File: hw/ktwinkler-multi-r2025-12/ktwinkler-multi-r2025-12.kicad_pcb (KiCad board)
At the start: 4 copper layers, 64 x 58 mm, 93 parts, among them J1 USB_C_Receptacle_USB2.0_16P, J10 Conn_01x06, J11 Conn_01x02, J12 Connector_HAN_P1, J13 Conn_01x02, J14 Conn_01x02, J15 Conn_01x02, J16 Conn_01x02, J17 Conn_01x02, J18 Conn_01x02, J19 Conn_01x06, J2 Conn_01x02, J4 Conn_01x02, J5 Conn_01x03, J6 Conn_01x02, J7 Conn_01x02, J8 Conn_01x02, J9 BWU.FL-IPEX1, Q1 HL3400A, Q3 HL2301A, Q4 HL3400A, SW1 RESET, SW2 BOOT, SW5 MODE, U1 TPS631000DRLR, U2 FM116C, U3 ESP32-C3FH4, U4 T1016H, U5 AD116, U6 Protection_H5VU25UC, U8 CH584F, U9 GM8023B, Y1 40M, Y2 32k, Y4 32k, Y5 32M

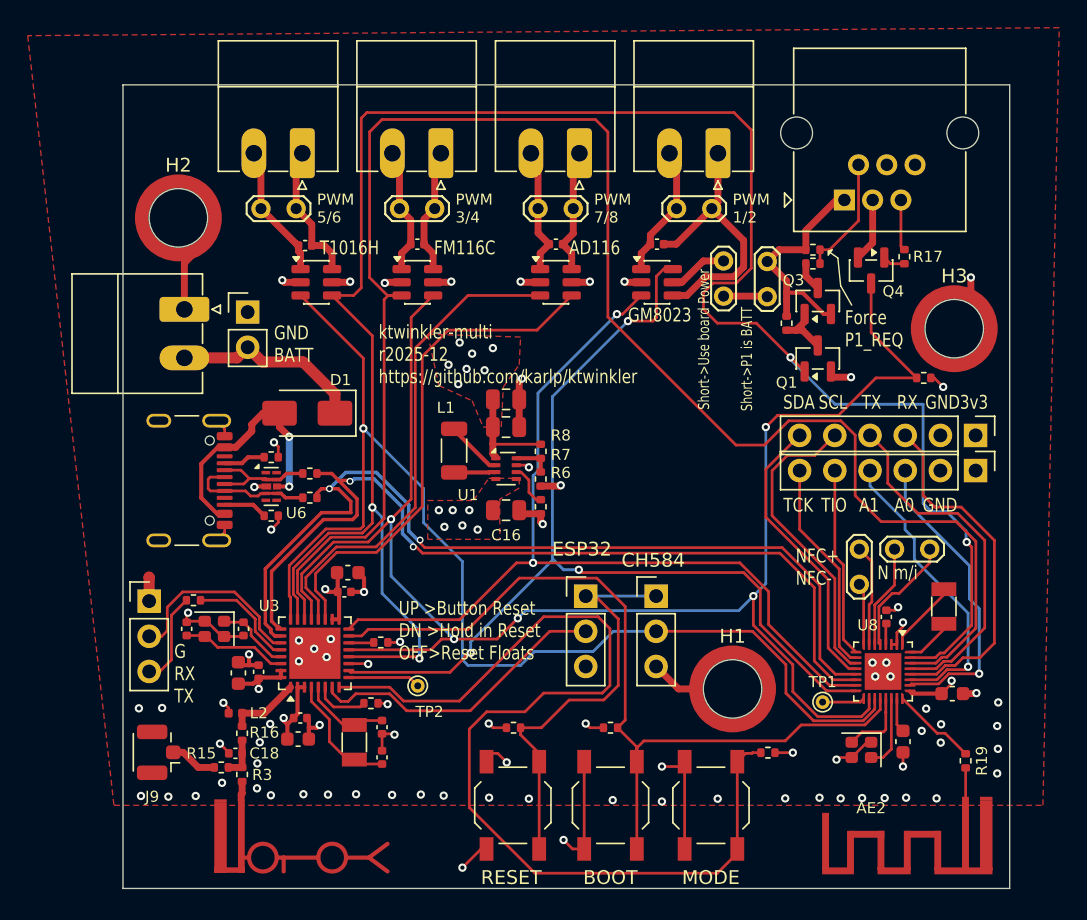
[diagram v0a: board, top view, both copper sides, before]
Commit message: hw: update to kicad 10 and order
We added a late qwiic connector to the ch584 side, why not, try that out
too.  We also fixed our smtso footprint, we hope...

Fuck poking the rf more, we're yolo-poling...
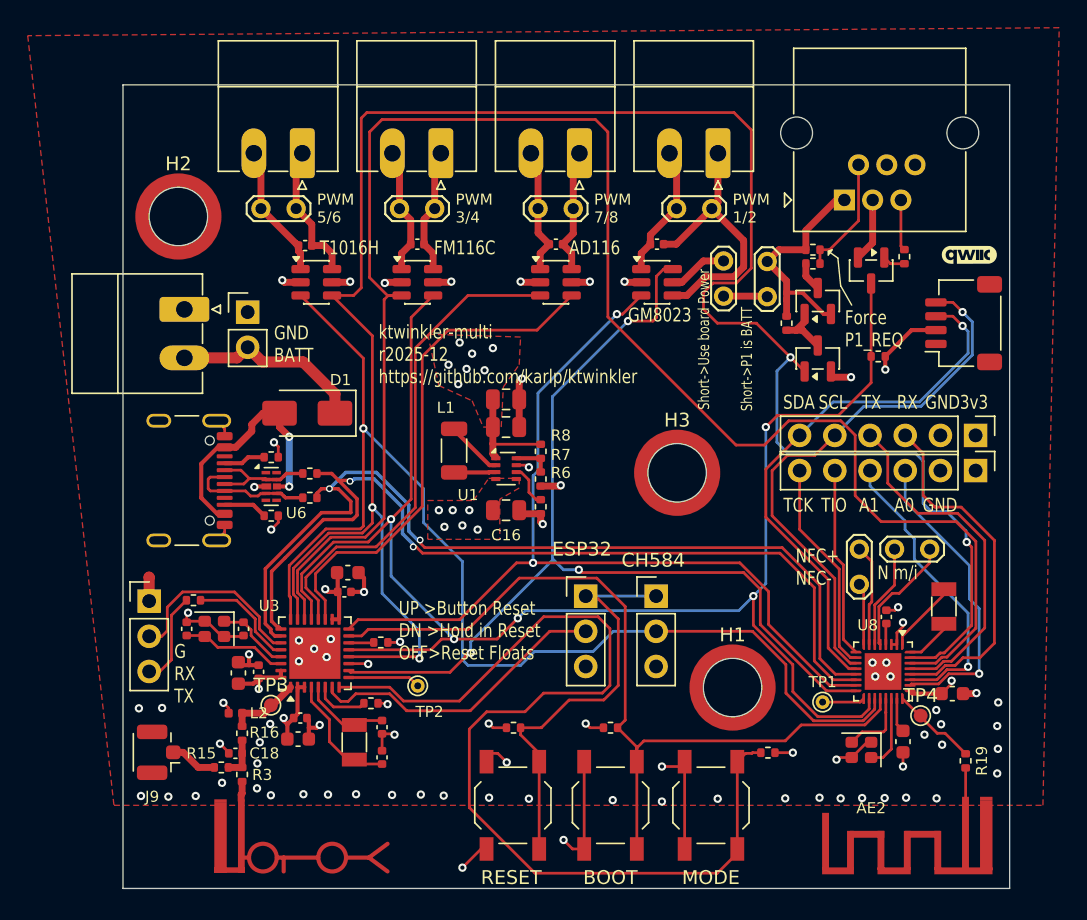
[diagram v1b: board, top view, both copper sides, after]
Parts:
- added G1: qwiic_Logo, SparkFun-Qwiic:qwiic_4mm, F.Cu at (161.1, 104.3)
- added J3: Conn_01x04, Connector_JST:JST_SH_SM04B-SRSS-TB_1x04-1MP_P1.00mm_Horizontal, F.Cu at (160.7, 109.2)
- added TP3: TestPoint, TestPoint:TestPoint_Pad_D1.0mm, F.Cu at (110.7, 136.8)
- added TP4: TestPoint, TestPoint:TestPoint_Pad_D1.0mm, F.Cu at (157.6, 137.5)
- H1, H2, H3: footprint jlc-extras:Mounting_SMTSO_M3_ALT -> jlc-extras:Mounting_SMTSO_M3_ALT2
- moved H3 22.5 mm to (140.0, 120.0)
- moved R18 3.64 mm to (154.5, 111.6)
- moved H1 0.10 mm to (144.0, 135.5)
- moved H2 0.10 mm to (104.0, 101.5)
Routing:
- net /ch584/TWI_SDA: track 20.9 -> 39.8 mm, vias 0 -> 1
- net /ch584/TWI_SCL: track 22.2 -> 40.2 mm, vias 0 -> 1
- net GND: track 81.6 -> 70.5 mm, vias 74 -> 73
- net /ch584/PWM3: track 119.0 -> 114.6 mm
- net +3V3: track 30.6 -> 34.8 mm
- net /ch584/PWM5: track 148.5 -> 151.1 mm

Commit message: hw/ktwinkler-multi: fix the bi/uni tvs fuckup
We're not likely to make a new version of _exactly_ this board, but
don't leave the totally busted short circuit around to stumble on later!
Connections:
- U6 pad 8: /power/VBUS -> GND
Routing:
- net /power/VBUS: track 18.6 -> 12.1 mm, vias 2 -> 0
- net GND: track 70.5 -> 71.3 mm
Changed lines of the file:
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@@
 			)
 		)
+		(attr exclude_from_bom)
 		(duplicate_pad_numbers_are_jumpers no)
 		(fp_circle
@@
 			(unit
 				(name "A")
-				(pins "1" "2" "4" "5" "8" "3" "6" "9" "7" "10")
+				(pins "1" "2" "4" "5" "3" "8" "6" "7" "9" "10")
 			)
 		)
@@
 			(net "GND")
 			(pinfunction "GND_3")
-			(pintype "passive")
+			(pintype "power_in")
 		)
 		(pad "4" smd rect
@@
 			(size 0.45 0.575)
 			(layers "F.Cu" "F.Mask" "F.Paste")
-			(net "/power/VBUS")
-			(pinfunction "VBUS_8")
+			(net "GND")
+			(pinfunction "GND_8")
 			(pintype "passive")
 		)
@@
 			)
 		)
+		(attr exclude_from_bom)
 		(duplicate_pad_numbers_are_jumpers no)
 		(fp_line
@@
 			)
 		)
+		(attr exclude_from_bom)
 		(duplicate_pad_numbers_are_jumpers no)
 		(fp_circle
@@
 			)
 		)
+		(attr dnp)
 		(duplicate_pad_numbers_are_jumpers no)
 		(fp_line
@@
 			)
 		)
+		(attr exclude_from_bom)
 		(net_tie_pad_groups "1,2")
 		(duplicate_pad_numbers_are_jumpers no)
@@
 			)
 		)
+		(attr exclude_from_bom)
 		(duplicate_pad_numbers_are_jumpers no)
 		(fp_line
@@
 			)
 		)
+		(attr exclude_from_bom)
 		(duplicate_pad_numbers_are_jumpers no)
 		(fp_line
@@
 			)
 		)
+		(attr exclude_from_bom)
 		(net_tie_pad_groups "1,2")
 		(duplicate_pad_numbers_are_jumpers no)
@@
 			)
 		)
+		(attr exclude_from_bom)
 		(duplicate_pad_numbers_are_jumpers no)
 		(fp_line
@@
 			)
 		)
+		(attr exclude_from_bom)
 		(duplicate_pad_numbers_are_jumpers no)
 		(fp_line
@@
 			)
 		)
+		(attr dnp)
 		(duplicate_pad_numbers_are_jumpers no)
 		(fp_circle
@@
 			)
 		)
+		(attr exclude_from_bom)
 		(duplicate_pad_numbers_are_jumpers no)
 		(fp_circle
@@
 			)
 		)
+		(attr exclude_from_bom)
 		(duplicate_pad_numbers_are_jumpers no)
 		(fp_line
@@
 			)
 		)
-		(attr board_only)
+		(attr board_only exclude_from_bom)
 		(duplicate_pad_numbers_are_jumpers no)
 		(fp_poly
@@
 			)
 		)
+		(attr exclude_from_bom)
 		(duplicate_pad_numbers_are_jumpers no)
 		(fp_line
@@
 	)
 	(segment
+		(start 111.9875 120.9875)
+		(end 112 121)
+		(width 0.3)
+		(layer "F.Cu")
+		(net "GND")
+	)
+	(segment
 		(start 154.11 103.4025)
 		(end 153.05 104.4625)
@@
 	)
 	(segment
+		(start 111.1125 120.9875)
+		(end 111.9875 120.9875)
+		(width 0.3)
+		(layer "F.Cu")
+		(net "GND")
+	)
+	(segment
 		(start 151.65 140.55)
 		(end 151.5 140.7)
@@
 	)
 	(segment
-		(start 110.35 120.9875)
-		(end 109.519144 120.9875)
-		(width 0.3)
-		(layer "F.Cu")
-		(net "GND")
-	)
-	(segment
 		(start 126.24 147.15)
 		(end 125.85 147.15)
@@
 	)
 	(segment
+		(start 110.35 120.9875)
+		(end 111.1125 120.9875)
+		(width 0.2)
+		(layer "F.Cu")
+		(net "GND")
+	)
+	(segment
 		(start 107.63 136.98)
 		(end 107.25 136.6)
@@
 	)
 	(segment
-		(start 109.519144 120.9875)
-		(end 109.480846 121.025798)
-		(width 0.3)
-		(layer "F.Cu")
-		(net "GND")
-	)
-	(segment
 		(start 104.6 130.785)
 		(end 104.6 130.2)
@@
 	)
 	(via
-		(at 109.480846 121.025798)
+		(at 112.05 121)
 		(size 0.6)
 		(drill 0.3)
@@
 	)
 	(segment
-		(start 108.721567 120.81)
-		(end 109.118067 120.4135)
-		(width 0.2)
-		(layer "F.Cu")
-		(net "/power/DMinusIn")
-	)
-	(segment
 		(start 112.98 120.05)
 		(end 111.8 120.05)
@@
 	)
 	(segment
-		(start 107.34 119.81)
-		(end 108.514567 119.81)
-		(width 0.2)
-		(layer "F.Cu")
-		(net "/power/DMinusIn")
-	)
-	(segment
 		(start 107.34 120.81)
 		(end 108.721567 120.81)
@@
 	)
 	(segment
-		(start 111.3625 120.4875)
-		(end 111.0875 120.4875)
-		(width 0.25)
+		(start 108.366567 119.81)
+		(end 107.34 119.81)
+		(width 0.2)
 		(layer "F.Cu")
 		(net "/power/DMinusIn")
 	)
 	(segment
-		(start 109.118067 120.4135)
-		(end 110.2635 120.4135)
+		(start 109.044067 120.4875)
+		(end 108.366567 119.81)
 		(width 0.2)
 		(layer "F.Cu")
@@
 	)
 	(segment
-		(start 108.514567 119.81)
-		(end 109.118067 120.4135)
-		(width 0.2)
+		(start 111.3625 120.4875)
+		(end 111.0875 120.4875)
+		(width 0.25)
 		(layer "F.Cu")
 		(net "/power/DMinusIn")
 	)
 	(segment
-		(start 110.3125 120.4875)
-		(end 111.0875 120.4875)
-		(width 0.25)
+		(start 108.721567 120.81)
+		(end 109.044067 120.4875)
+		(width 0.2)
 		(layer "F.Cu")
 		(net "/power/DMinusIn")
@@
 	(segment
 		(start 110.3125 120.4875)
-		(end 110.3125 120.4625)
+		(end 111.0875 120.4875)
 		(width 0.25)
 		(layer "F.Cu")
@@
 	)
 	(segment
-		(start 110.2635 120.4135)
-		(end 110.3125 120.4625)
+		(start 109.044067 120.4875)
+		(end 110.3125 120.4875)
 		(width 0.2)
 		(layer "F.Cu")
@@
 	)
 	(segment
-		(start 111.9875 120.9875)
-		(end 112 121)
-		(width 0.3)
-		(layer "F.Cu")
-		(net "/power/VBUS")
-	)
-	(segment
 		(start 105.65 121.808281)
 		(end 106.801719 122.96)
@@
 	)
 	(segment
-		(start 111.1125 120.9875)
-		(end 111.9875 120.9875)
-		(width 0.3)
-		(layer "F.Cu")
-		(net "/power/VBUS")
-	)
-	(segment
 		(start 110.1 115.7)
 		(end 111.3 115.7)
@@
 	)
 	(segment
-		(start 111.3 116.7)
-		(end 112 117.4)
-		(width 0.5)
-		(layer "F.Cu")
-		(net "/power/VBUS")
-	)
-	(segment
 		(start 107.34 118.16)
 		(end 106.84 118.16)
@@
 	)
 	(segment
-		(start 111.3 115.7)
-		(end 111.3 116.7)
-		(width 0.5)
-		(layer "F.Cu")
-		(net "/power/VBUS")
-	)
-	(via
-		(at 112 117.4)
-		(size 0.6)
-		(drill 0.3)
-		(layers "F.Cu" "B.Cu")
-		(capping no)
-		(covering
-			(front no)
-			(back no)
-		)
-		(plugging
-			(front no)
-			(back no)
-		)
-		(filling no)
-		(net "/power/VBUS")
-	)
-	(via
-		(at 112 121)
-		(size 0.6)
-		(drill 0.3)
-		(layers "F.Cu" "B.Cu")
-		(capping no)
-		(covering
-			(front no)
-			(back no)
-		)
-		(plugging
-			(front no)
-			(back no)
-		)
-		(filling no)
-		(net "/power/VBUS")
-	)
-	(segment
-		(start 112 117.4)
-		(end 112 121)
-		(width 0.5)
-		(layer "B.Cu")
-		(net "/power/VBUS")
-	)
-	(segment
 		(start 111.865 138.155)
 		(end 111.6 137.89)
@@
 	)
 	(segment
-		(start 107.34 121.31)
-		(end 108.845809 121.31)
+		(start 110.2875 121.5125)
+		(end 110.3125 121.4875)
 		(width 0.2)
 		(layer "F.Cu")
@@
 	)
 	(segment
-		(start 110.2875 121.5125)
-		(end 110.3125 121.4875)
-		(width 0.2)
-		(layer "F.Cu")
-		(net "/power/DPlusIn")
-	)
-	(segment
 		(start 111.725 121.8)
 		(end 111.625 121.7)
@@
 	)
 	(segment
-		(start 109.913383 121.5125)
-		(end 110.2875 121.5125)
+		(start 109.035 121.31)
+		(end 109.2375 121.5125)
 		(width 0.2)
 		(layer "F.Cu")
@@
 	)
 	(segment
-		(start 109.211607 121.675798)
-		(end 109.750085 121.675798)
-		(width 0.2)
-		(layer "F.Cu")
-		(net "/power/DPlusIn")
-	)
-	(segment
 		(start 106.15 120.45)
 		(end 106.29 120.31)
@@
 	)
 	(segment
-		(start 109.750085 121.675798)
-		(end 109.913383 121.5125)
-		(width 0.2)
-		(layer "F.Cu")
-		(net "/power/DPlusIn")
-	)
-	(segment
 		(start 106.31 121.31)
 		(end 106.15 121.15)
@@
 	)
 	(segment
-		(start 108.845809 121.31)
-		(end 109.211607 121.675798)
+		(start 109.2375 121.5125)
+		(end 110.2875 121.5125)
 		(width 0.2)
 		(layer "F.Cu")
@@
 		(layer "F.Cu")
 		(net "/power/DPlusIn")
+	)
+	(segment
+		(start 107.34 121.31)
+		(end 109.035 121.31)
+		(width 0.2)
+		(layer "F.Cu")
+		(net "/power/DPlusIn")
